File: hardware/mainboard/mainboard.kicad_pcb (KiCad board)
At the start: 2 copper layers, 3 parts, among them J1 2309407-1, J2 WP7B-S040VA1-R6000, J3 WP7B-S040VA1-R6000

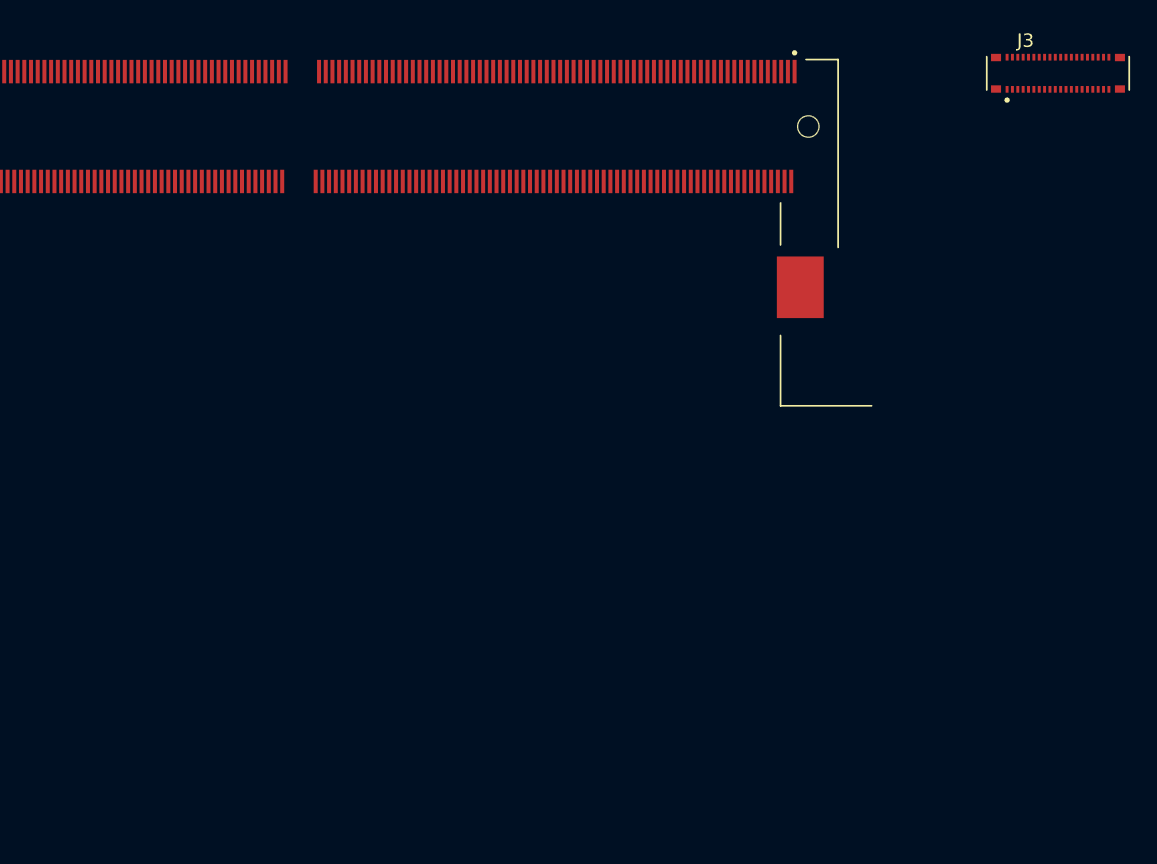
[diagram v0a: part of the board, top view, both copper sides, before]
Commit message: footprints assigned, ready to begin pcb design
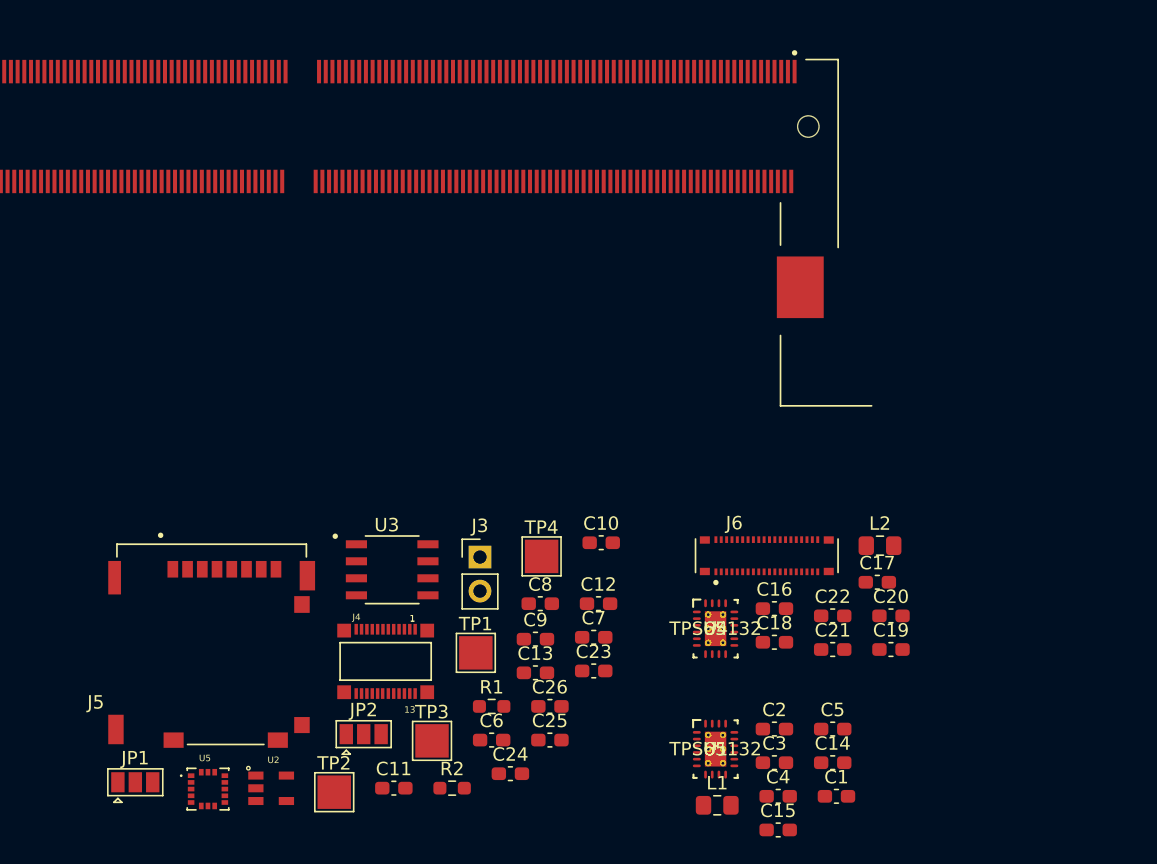
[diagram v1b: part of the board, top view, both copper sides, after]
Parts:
- added C1: 4.7uF, Capacitor_SMD:C_0603_1608Metric_Pad1.08x0.95mm_HandSolder, F.Cu at (134.0, 175.0)
- added C10: 100nF, Capacitor_SMD:C_0603_1608Metric_Pad1.08x0.95mm_HandSolder, F.Cu at (116.4, 156.1)
- added C11: 4.7uF, Capacitor_SMD:C_0603_1608Metric_Pad1.08x0.95mm_HandSolder, F.Cu at (101.0, 174.4)
- added C12: 100nF, Capacitor_SMD:C_0603_1608Metric_Pad1.08x0.95mm_HandSolder, F.Cu at (116.2, 160.6)
- added C13: 1uF, Capacitor_SMD:C_0603_1608Metric_Pad1.08x0.95mm_HandSolder, F.Cu at (111.5, 165.8)
- added C14: 100nF, Capacitor_SMD:C_0603_1608Metric_Pad1.08x0.95mm_HandSolder, F.Cu at (133.7, 172.5)
- added C15: 10nF, Capacitor_SMD:C_0603_1608Metric_Pad1.08x0.95mm_HandSolder, F.Cu at (129.7, 177.5)
- added C16: 100nF, Capacitor_SMD:C_0603_1608Metric_Pad1.08x0.95mm_HandSolder, F.Cu at (129.4, 161.0)
- added C17: 10nF, Capacitor_SMD:C_0603_1608Metric_Pad1.08x0.95mm_HandSolder, F.Cu at (137.1, 159.0)
- added C18: 4.7uF, Capacitor_SMD:C_0603_1608Metric_Pad1.08x0.95mm_HandSolder, F.Cu at (129.4, 163.5)
- added C19: 4.7uF, Capacitor_SMD:C_0603_1608Metric_Pad1.08x0.95mm_HandSolder, F.Cu at (138.1, 164.0)
- added C2: 4.7uF, Capacitor_SMD:C_0603_1608Metric_Pad1.08x0.95mm_HandSolder, F.Cu at (129.4, 170.0)
- added C20: 2.2uF, Capacitor_SMD:C_0603_1608Metric_Pad1.08x0.95mm_HandSolder, F.Cu at (138.1, 161.5)
- added C21: 4.7uF, Capacitor_SMD:C_0603_1608Metric_Pad1.08x0.95mm_HandSolder, F.Cu at (133.7, 164.0)
- added C22: 4.7uF, Capacitor_SMD:C_0603_1608Metric_Pad1.08x0.95mm_HandSolder, F.Cu at (133.7, 161.5)
- added C23: 0.1uF, Capacitor_SMD:C_0603_1608Metric_Pad1.08x0.95mm_HandSolder, F.Cu at (115.9, 165.6)
- added C24: 2.2uF, Capacitor_SMD:C_0603_1608Metric_Pad1.08x0.95mm_HandSolder, F.Cu at (109.7, 173.3)
- added C25: 10nF, Capacitor_SMD:C_0603_1608Metric_Pad1.08x0.95mm_HandSolder, F.Cu at (112.6, 170.8)
- added C26: 0.1uF, Capacitor_SMD:C_0603_1608Metric_Pad1.08x0.95mm_HandSolder, F.Cu at (112.6, 168.3)
- added C3: 2.2uF, Capacitor_SMD:C_0603_1608Metric_Pad1.08x0.95mm_HandSolder, F.Cu at (129.4, 172.5)
- added C4: 4.7uF, Capacitor_SMD:C_0603_1608Metric_Pad1.08x0.95mm_HandSolder, F.Cu at (129.7, 175.0)
- added C5: 4.7uF, Capacitor_SMD:C_0603_1608Metric_Pad1.08x0.95mm_HandSolder, F.Cu at (133.7, 170.0)
- added C6: 1uF, Capacitor_SMD:C_0603_1608Metric_Pad1.08x0.95mm_HandSolder, F.Cu at (108.3, 170.8)
- added C7: 1uF, Capacitor_SMD:C_0603_1608Metric_Pad1.08x0.95mm_HandSolder, F.Cu at (115.9, 163.1)
- added C8: 100nF, Capacitor_SMD:C_0603_1608Metric_Pad1.08x0.95mm_HandSolder, F.Cu at (111.9, 160.6)
- added C9: 10nF, Capacitor_SMD:C_0603_1608Metric_Pad1.08x0.95mm_HandSolder, F.Cu at (111.5, 163.3)
- added J4: AXK7L24223G, mainboard:PANASONIC_AXK7L24223G, F.Cu at (100.3, 164.9)
- added J5: 503182-1852, mainboard:MOLEX_503182-1852, F.Cu at (87.4, 164.4)
- added J6: WP7B-S040VA1-R6000, mainboard:JAE_WP7B-S040VA1-R6000, F.Cu at (128.8, 157.0)
- added JP1: BL_SELECT, Jumper:SolderJumper-3_P1.3mm_Open_Pad1.0x1.5mm, F.Cu at (81.7, 173.9)
- added JP2: BL_SELECT, Jumper:SolderJumper-3_P1.3mm_Open_Pad1.0x1.5mm, F.Cu at (98.7, 170.4)
- added L1: 2.2uH, Inductor_SMD:L_0805_2012Metric_Pad1.15x1.40mm_HandSolder, F.Cu at (125.1, 175.7)
- added L2: 2.2uH, Inductor_SMD:L_0805_2012Metric_Pad1.15x1.40mm_HandSolder, F.Cu at (137.2, 156.3)
- added R1: 60k, Resistor_SMD:R_0603_1608Metric_Pad0.98x0.95mm_HandSolder, F.Cu at (108.3, 168.3)
- added R2: 10k, Resistor_SMD:R_0603_1608Metric_Pad0.98x0.95mm_HandSolder, F.Cu at (105.3, 174.4)
- added TP1: TestPoint, TestPoint:TestPoint_Pad_2.5x2.5mm, F.Cu at (107.1, 164.3)
- added TP2: TestPoint, TestPoint:TestPoint_Pad_2.5x2.5mm, F.Cu at (96.5, 174.7)
- added TP3: TestPoint, TestPoint:TestPoint_Pad_2.5x2.5mm, F.Cu at (103.8, 170.9)
- added TP4: TestPoint, TestPoint:TestPoint_Pad_2.5x2.5mm, F.Cu at (112.0, 157.1)
- added U1: TPS65132, mainboard:TPS65132WRVCT, F.Cu at (125.0, 171.5)
- added U2: MIC5504-1.2YM5-TR, mainboard:SOT23-5P95_280X145XL45X37N, F.Cu at (91.8, 174.4)
- added U3: MCP1725-ADJE_MC, mainboard:SOIC127P599X175-8N, F.Cu at (100.8, 158.1)
- added U4: TPS65132, mainboard:TPS65132WRVCT, F.Cu at (125.0, 162.5)
- added U5: ICM-20602, mainboard:PQFN50P300X300X80-16N, F.Cu at (87.1, 174.5)
- J3: value WP7B-S040VA1-R6000 -> Conn_01x02_Male; footprint mainboard:JAE_WP7B-S040VA1-R6000 -> Connector_PinHeader_2.54mm:PinHeader_1x02_P2.54mm_Vertical
- moved J3 56.3 mm to (107.4, 157.1)
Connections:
- J1 pad 100: (no net) -> /SDMMC0_D1
- J1 pad 101: (no net) -> /MIPI_CSI0_PWN
- J1 pad 102: (no net) -> /SDMMC0_D2
- J1 pad 103: (no net) -> /MIPI_CSI1_RST
- J1 pad 104: (no net) -> /SDMMC0_D3
- J1 pad 106: (no net) -> /SDMMC0_CMD
- J1 pad 107: (no net) -> /VCC1V8_CAM
- J1 pad 108: (no net) -> /SDMMC0_DET_L
- J1 pad 111: (no net) -> /GPIO2_B3_CIF_CLKOUTA
- J1 pad 112: (no net) -> /SDMMC0_CLK
- J1 pad 115: (no net) -> /MIPI_RX0_D3N
- J1 pad 116: (no net) -> /MIPI_TX1_D0N
- J1 pad 117: (no net) -> /MIPI_RX0_D3P
- J1 pad 118: (no net) -> /MIPI_TX1_D0P
- J1 pad 121: (no net) -> /MIPI_RX0_D2N
- J1 pad 122: (no net) -> /MIPI_TX1_D1N
- J1 pad 123: (no net) -> /MIPI_RX0_D2P
- J1 pad 124: (no net) -> /MIPI_TX1_D1P
- J1 pad 127: (no net) -> /MIPI_RX0_CLKN
- J1 pad 128: (no net) -> /MIPI_TX1_CLKN
- J1 pad 129: (no net) -> /MIPI_RX0_CLKP
- J1 pad 130: (no net) -> /MIPI_TX1_CLKP
- J1 pad 133: (no net) -> /MIPI_RX0_D1N
- J1 pad 134: (no net) -> /MIPI_TX1_D2N
- J1 pad 135: (no net) -> /MIPI_RX0_D1P
- J1 pad 136: (no net) -> /MIPI_TX1_D2P
- J1 pad 139: (no net) -> /MIPI_RX0_D0N
- J1 pad 141: (no net) -> /MIPI_RX0_D0P
- J1 pad 148: (no net) -> /MIPI_TX0_D3N
- J1 pad 150: (no net) -> /MIPI_TX0_D3P
- J1 pad 154: (no net) -> /MIPI_TX0_D2N
- J1 pad 156: (no net) -> /MIPI_TX0_D2P
- J1 pad 160: (no net) -> /MIPI_TX0_CLKN
- J1 pad 162: (no net) -> /MIPI_TX0_CLKP
- J1 pad 166: (no net) -> /MIPI_TX0_D1N
- J1 pad 168: (no net) -> /MIPI_TX0_D1P
- J1 pad 172: (no net) -> /MIPI_TX0_D0N
- J1 pad 174: (no net) -> /MIPI_TX0_D0P
- J1 pad 37: (no net) -> /RESX_0
- J1 pad 39: (no net) -> /RESX_1
- J1 pad 41: (no net) -> /GPIO_BL
- J1 pad 53: (no net) -> /I2C1_SCL
- J1 pad 55: (no net) -> /I2C1_SDA
- J1 pad 57: (no net) -> /I2C2_SDA
- J1 pad 59: (no net) -> /I2C2_SCL
- J1 pad 88: (no net) -> /PWM0_BL
- J1 pad 98: (no net) -> /SDMMC0_D0
- J1 pad SH1: Net-(J1-PadSH1) -> GND
- J1 pad SH2: Net-(J1-PadSH1) -> GND
- J2 pad 1: (no net) -> /MIPI_TX0_D3N
- J2 pad 10: (no net) -> /MIPI_TX0_D2P
- J2 pad 2: (no net) -> /MIPI_TX0_D3P
- J2 pad 22: (no net) -> /LCD 1/AVDD
- J2 pad 29: (no net) -> /RESX_0
- J2 pad 3: (no net) -> /MIPI_TX0_D0N
- J2 pad 32: (no net) -> /LCD 1/LEDPWM
- J2 pad 36: (no net) -> /LCD 1/AVEE
- J2 pad 37: (no net) -> GND
- J2 pad 38: (no net) -> GND
- J2 pad 39: (no net) -> +2V8
- J2 pad 4: (no net) -> /MIPI_TX0_D0P
- J2 pad 40: (no net) -> +2V8
- J2 pad 5: (no net) -> /MIPI_TX0_CLKN
- J2 pad 6: (no net) -> /MIPI_TX0_CLKP
- J2 pad 7: (no net) -> /MIPI_TX0_D1N
- J2 pad 8: (no net) -> /MIPI_TX0_D1P
- J2 pad 9: (no net) -> /MIPI_TX0_D2N
- J3 pad 1: (no net) -> +5V
- J3 pad 2: (no net) -> GND

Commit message: mipi done, power almost done
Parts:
- removed TP2: TestPoint, TestPoint:TestPoint_Pad_2.5x2.5mm
- added H1: MountingHole, MountingHole:MountingHole_2.2mm_M2_Pad_Via, F.Cu at (91.2, 94.5)
- added H2: MountingHole, MountingHole:MountingHole_2.2mm_M2_Pad_Via, F.Cu at (187.2, 69.5)
- added H3: MountingHole, MountingHole:MountingHole_2.2mm_M2_Pad_Via, F.Cu at (187.2, 94.5)
- added H4: MountingHole, MountingHole:MountingHole_2.2mm_M2_Pad_Via, F.Cu at (91.2, 69.5)
- C1, C10, C11, C12, C13, C14, C15, C16, C17, C18, C19, C2, C20, C21, C22, C23, C24, C25, C26, C3, C4, C5, C6, C7, C8, C9: footprint Capacitor_SMD:C_0603_1608Metric_Pad1.08x0.95mm_HandSolder -> Capacitor_SMD:C_0402_1005Metric_Pad0.74x0.62mm_HandSolder
- R1, R2: footprint Resistor_SMD:R_0603_1608Metric_Pad0.98x0.95mm_HandSolder -> Resistor_SMD:R_0402_1005Metric_Pad0.72x0.64mm_HandSolder
- TP1, TP3, TP4: footprint TestPoint:TestPoint_Pad_2.5x2.5mm -> TestPoint:TestPoint_Pad_D1.0mm
- moved J5 125.9 mm to (182.5, 82.0), turned to 90 degrees
- moved JP2 124.5 mm to (152.8, 58.2), turned to 180 degrees
- moved JP1 123.4 mm to (114.5, 55.0), turned to 90 degrees
- moved U5 121.7 mm to (153.9, 72.8), turned to 90 degrees
- moved C4 117.4 mm to (103.5, 60.5), turned to 180 degrees
- moved U2 115.8 mm to (145.4, 71.8), turned to 90 degrees
- moved C3 113.4 mm to (103.0, 62.2), turned to 270 degrees
- moved J2 110.2 mm to (108.2, 70.0)
- moved L1 107.8 mm to (158.0, 73.0), turned to 270 degrees
- moved C1 107.6 mm to (158.7, 70.3), turned to 180 degrees
- moved TP1 106.0 mm to (152.9, 68.7)
- moved TP3 102.8 mm to (122.3, 69.7)
- moved J4 102.4 mm to (139.2, 70.2), turned to 180 degrees
- moved C7 101.4 mm to (155.0, 69.6), turned to 270 degrees
- moved C2 100.3 mm to (106.6, 72.3)
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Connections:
- net /MIPI_RX0_CLKN renamed /MIPI_RX0_CLK-
- net /MIPI_RX0_CLKP renamed /MIPI_RX0_CLK+
- net /MIPI_RX0_D0N renamed /MIPI_RX0_D0-
- net /MIPI_RX0_D0P renamed /MIPI_RX0_D0+
- net /MIPI_RX0_D1N renamed /MIPI_RX0_D1-
- net /MIPI_RX0_D1P renamed /MIPI_RX0_D1+
- net /MIPI_RX0_D2N renamed /MIPI_RX0_D2-
- net /MIPI_RX0_D2P renamed /MIPI_RX0_D2+
- net /MIPI_RX0_D3N renamed /MIPI_RX0_D3-
- net /MIPI_RX0_D3P renamed /MIPI_RX0_D3+
- net /MIPI_TX0_CLKN renamed /MIPI_TX0_CLK-
- net /MIPI_TX0_CLKP renamed /MIPI_TX0_CLK+
- net /MIPI_TX0_D0N renamed /MIPI_TX0_D0-
- net /MIPI_TX0_D0P renamed /MIPI_TX0_D0+
- net /MIPI_TX0_D1N renamed /MIPI_TX0_D1-
- net /MIPI_TX0_D1P renamed /MIPI_TX0_D1+
- net /MIPI_TX0_D2N renamed /MIPI_TX0_D2-
- net /MIPI_TX0_D2P renamed /MIPI_TX0_D2+
- net /MIPI_TX1_CLKN renamed /MIPI_TX1_CLK-
- net /MIPI_TX1_CLKP renamed /MIPI_TX1_CLK+
- net /MIPI_TX1_D0N renamed /MIPI_TX1_D0-
- net /MIPI_TX1_D0P renamed /MIPI_TX1_D0+
- net /MIPI_TX1_D1N renamed /MIPI_TX1_D1-
- net /MIPI_TX1_D1P renamed /MIPI_TX1_D1+
- net /MIPI_TX1_D2N renamed /MIPI_TX1_D2-
- net /MIPI_TX1_D2P renamed /MIPI_TX1_D2+
- C1 pad 1: +5V -> +3V3
- C11 pad 1: +5V -> +3V3
- C14 pad 1: +5V -> +3V3
- C15 pad 1: +5V -> +3V3
- C16 pad 1: +5V -> +3V3
- C17 pad 1: +5V -> +3V3
- C18 pad 1: +5V -> +3V3
- J1 pad 107: /VCC1V8_CAM -> (no net)
- J1 pad 140: (no net) -> /MIPI_TX1_D3-
- J1 pad 142: (no net) -> /MIPI_TX1_D3+
- J1 pad 148: /MIPI_TX0_D3N -> /MIPI_TX0_D3-
- J1 pad 150: /MIPI_TX0_D3P -> /MIPI_TX0_D3+
- J2 pad 1: /MIPI_TX0_D3N -> /MIPI_TX0_D3-
- J2 pad 2: /MIPI_TX0_D3P -> /MIPI_TX0_D3+
- J4 pad 3: /VCC1V8_CAM -> +1V8
- J6 pad 1: /MIPI_TX0_D3N -> /MIPI_TX1_D3-
- J6 pad 2: /MIPI_TX0_D3P -> /MIPI_TX1_D3+
- L1 pad 1: +5V -> +3V3
- L2 pad 1: +5V -> +3V3
- U1 pad 4: +5V -> +3V3
- U3 pad 1: +5V -> +3V3
- U3 pad 2: +5V -> +3V3
- U3 pad 3: +5V -> +3V3
- U4 pad 4: +5V -> +3V3
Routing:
- net GND: track 0.00 -> 73.8 mm, vias 0 -> 19
- net /MIPI_TX1_D2+: track 0.00 -> 56.2 mm, vias 0 -> 2
- net /MIPI_TX1_D0+: track 0.00 -> 56.0 mm, vias 0 -> 2
- net /MIPI_TX1_D3+: track 0.00 -> 56.0 mm, vias 0 -> 2
- net /MIPI_TX1_D1+: track 0.00 -> 56.0 mm, vias 0 -> 2
- net /MIPI_TX1_CLK+: track 0.00 -> 56.0 mm, vias 0 -> 2
- net /MIPI_TX1_CLK-: track 0.00 -> 55.4 mm, vias 0 -> 2
- net /MIPI_TX1_D3-: track 0.00 -> 55.2 mm, vias 0 -> 2
- net /SDMMC0_DET_L: track 0.00 -> 55.1 mm
- net /MIPI_TX1_D2-: track 0.00 -> 55.0 mm, vias 0 -> 2
- net /MIPI_TX1_D1-: track 0.00 -> 54.4 mm, vias 0 -> 2
- net /MIPI_TX1_D0-: track 0.00 -> 54.2 mm, vias 0 -> 2
- net /SDMMC0_CLK: track 0.00 -> 46.3 mm, vias 0 -> 2
- net /SDMMC0_D1: track 0.00 -> 43.4 mm, vias 0 -> 2
- net /SDMMC0_D0: track 0.00 -> 43.3 mm, vias 0 -> 2
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- added copper zone on In2.Cu, net +3V3
- added copper zone on In1.Cu, net GND
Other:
- board outline added: 101 x 30 mm
- copper layers 2 -> 4
- net class Default: clearance 0.2 -> 0.127; trace_width 0.25 -> 0.254; via_dia 0.8 -> 0.6858; via_drill 0.4 -> 0.3302
- rule pad_to_mask_clearance: 0.05 -> 0
- rule trace_clearance: 0.2 -> 0.127
- rule trace_min: 0.2 -> 0.0889
- rule via_min_drill: 0.3 -> 0.2
- rule via_min_size: 0.4 -> 0.45

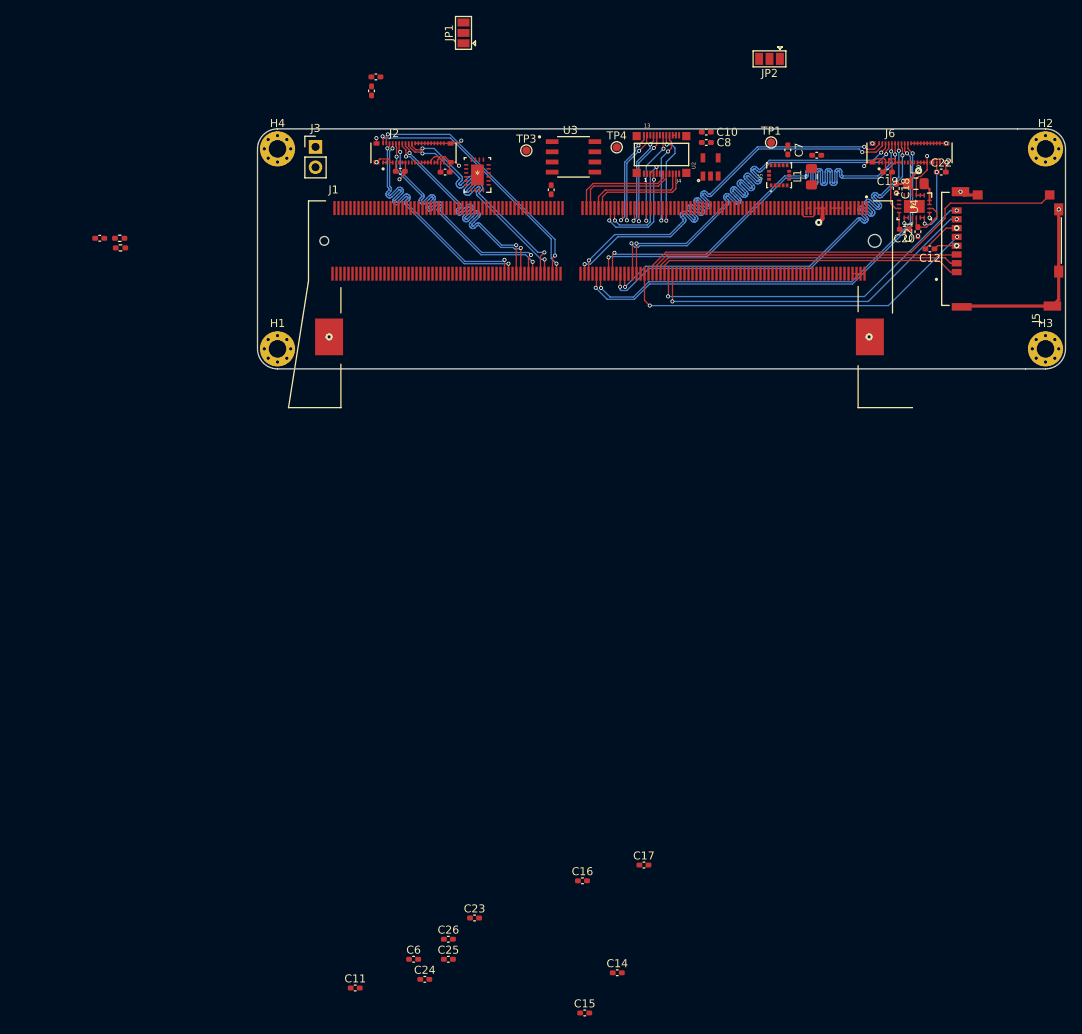
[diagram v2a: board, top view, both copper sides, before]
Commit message: 0.1 routing done, will merge after cleaning up silkscreen
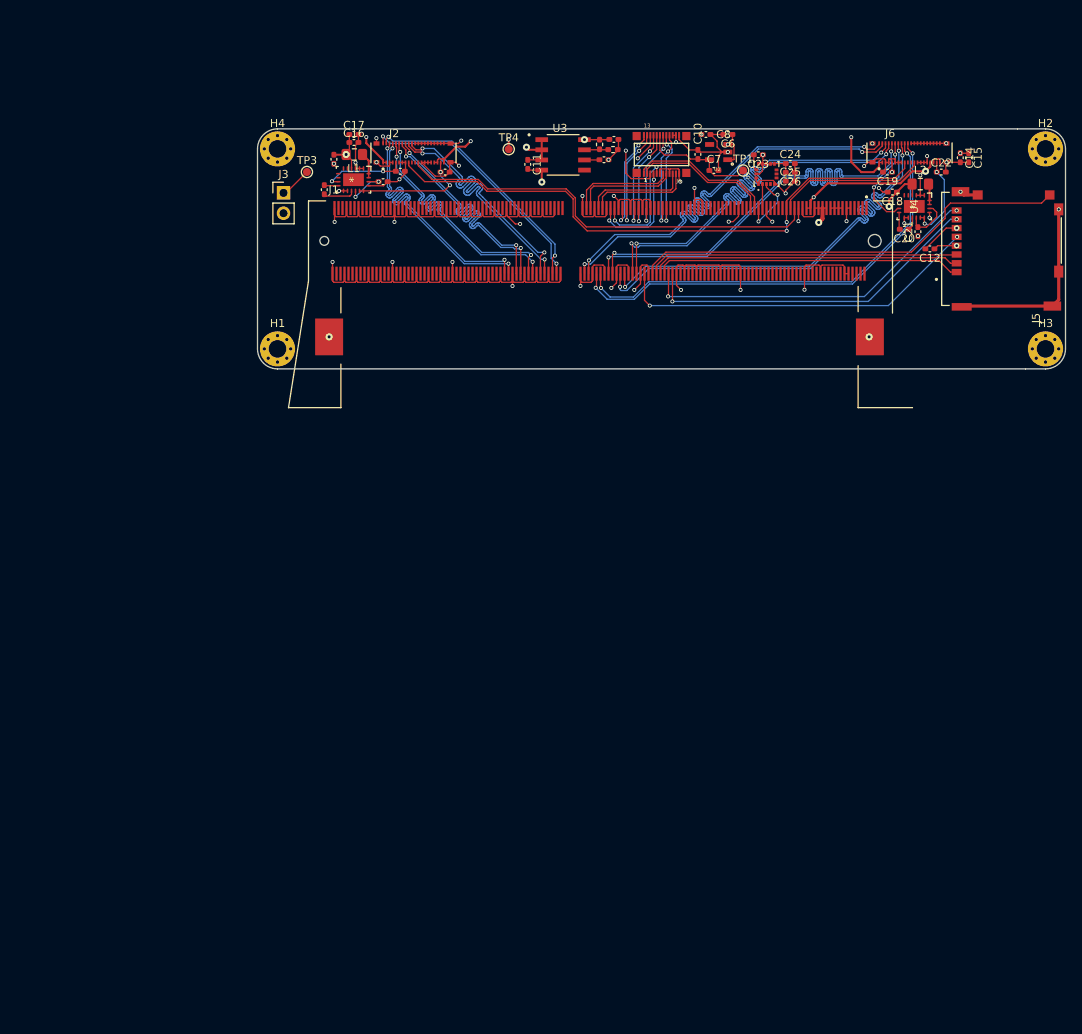
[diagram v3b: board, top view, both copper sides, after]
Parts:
- removed JP1, JP2: BL_SELECT, Jumper:SolderJumper-3_P1.3mm_Open_Pad1.0x1.5mm
- moved C15 117.2 mm to (177.7, 70.6), turned to 270 degrees
- moved C24 111.7 mm to (155.3, 71.3)
- moved C14 110.5 mm to (176.6, 70.6), turned to 270 degrees
- moved C6 110.3 mm to (147.6, 67.7), turned to 180 degrees
- moved C25 106.2 mm to (155.3, 73.5)
- moved C11 105.2 mm to (122.5, 71.4), turned to 270 degrees
- moved C26 104.9 mm to (155.3, 72.4), turned to 180 degrees
- moved C23 101.8 mm to (151.3, 70.2), turned to 180 degrees
- moved C17 98.3 mm to (100.8, 67.7)
- moved C16 96.6 mm to (100.8, 68.7)
- moved C9 63.8 mm to (132.1, 70.9), turned to 0 degrees
- moved R2 62.8 mm to (133.2, 69.6), turned to 0 degrees
- moved R1 61.1 mm to (131.5, 69.0), turned to 270 degrees
- moved C1 60.4 mm to (98.3, 70.8), turned to 270 degrees
- moved L1 57.2 mm to (100.8, 70.2), turned to 0 degrees
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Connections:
- J1 pad 1: +12V -> (no net)
- J1 pad 2: +12V -> (no net)
- J1 pad 3: +12V -> (no net)
- J1 pad 4: +12V -> (no net)
- J1 pad 5: +12V -> (no net)
- J1 pad 6: +12V -> (no net)
- J1 pad 7: +12V -> (no net)
- J1 pad 8: +12V -> (no net)
- J1 pad 88: /PWM0_BL -> (no net)
- J2 pad 32: /LCD 1/LEDPWM -> /GPIO_BL
- J3 pad 1: +5V -> +3V3
- J4 pad 1: /I2C1_SDA -> /I2C2_SDA
- J4 pad 2: /I2C1_SCL -> /I2C2_SCL
- J6 pad 32: /LCD 2/LEDPWM -> /GPIO_BL
- TP3 pad 1: +5V -> +3V3
- U5 pad 2: /I2C2_SCL -> /I2C1_SCL
- U5 pad 3: /I2C2_SDA -> /I2C1_SDA
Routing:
- net GND: track 73.8 -> 312.6 mm, vias 19 -> 49
- net +1V8: track 4.41 -> 108.8 mm, vias 0 -> 5
- net +2V8: track 1.20 -> 80.9 mm, vias 0 -> 6
- net /GPIO_BL: track 0.00 -> 73.3 mm, vias 0 -> 2
- net /RESX_0: track 0.00 -> 53.7 mm
- net +3V3: track 15.2 -> 38.3 mm, vias 3 -> 7
- net /RESX_1: track 0.00 -> 18.7 mm
- net /I2C2_SDA: track 0.00 -> 18.1 mm
- net /I2C2_SCL: track 0.00 -> 17.0 mm
- net +1V2: track 0.00 -> 14.7 mm
- net /LCD 1/AVDD: track 1.21 -> 14.9 mm, vias 0 -> 2
- net /LCD 1/AVEE: track 1.11 -> 10.4 mm, vias 0 -> 2
- net /I2C1_SDA: track 0.00 -> 8.16 mm, vias 0 -> 2
- net Net-(C4-Pad2): track 0.00 -> 5.65 mm, vias 0 -> 2
- net Net-(C3-Pad1): track 0.00 -> 4.03 mm
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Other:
- board text added: "© Krishna Mani 2020 MR Headset Mainboard v0.1"
